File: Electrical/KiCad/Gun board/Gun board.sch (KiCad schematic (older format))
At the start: 13 parts

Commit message: created 5v, 3v3, and 3v regulator circuits
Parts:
- added C? (x2): 4.7μF, symbol Device:C
- added C?: C, symbol Device:C
- added L?: 4.7μH, symbol Device:L
- added LD? (x5): Laserdiode_1C2A, symbol Device:Laserdiode_1C2A
- added R?: 1.02MΩ, symbol Device:R
- added R?: 332kΩ, symbol Device:R
- added R?: 1MΩ, symbol Device:R
- added R?: 270Ω, symbol Device:R
- added R?: 390Ω, symbol Device:R
- added SW?: SW_SPST, symbol Switch:SW_SPST
- added U?: AAT1217, SOT23-6, symbol aat1217.lib:AAT1217
- added U?: LM317_3PinPackage, symbol Regulator_Linear:LM317_3PinPackage
- C? (x2): value C -> 4.7μF
- D?: value D_Schottky -> MBR0520
- L?: value L -> 4.7μH
- Q?: value Q_PMOS_DGS -> Si2305 DS
- R? (x2): value R -> 510kΩ
- R?: value R -> 1.02MΩ
- R?: value R -> 332kΩ
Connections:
- net labels added: +3V, +5V, +BATT, 5V_SHDN, I2C_SCL, I2C_SDA, MISO, MOSI, SCK, SELECT, SYS_SWCLK, SYS_SWDIO, TRIGGER, VOLUME
- net labels removed: ON\OFF
- wire segments 27 -> 45
- no-connect marks 0 -> 1
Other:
- note added: "Laser Diode Array"
- moved on the sheet: BT?, C?, D?, L?, Q?, R?

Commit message: added power decoupling and nets
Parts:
- removed C? (x4): 4.7μF, symbol Device:C
- removed C?: C, symbol Device:C
- added C? (x2): 100nF, symbol Device:C
- added C? (x5): 4.7μF, symbol Device:CP
- added C? (x2): 1μF, symbol Device:CP
- added C?: 10nF, symbol Device:C
- added J?: Conn_01x05, symbol Connector_Generic:Conn_01x05
- added R?: 10kΩ, symbol Device:R
- U? (x2): symbol aat1217.lib:AAT1217 -> Gun-board-rescue:AAT1217-aat1217.lib
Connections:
- net labels added: CE, CSN, RESET, VDD, VDDA
- wire segments 45 -> 88
- no-connect marks 1 -> 0
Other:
- note added: "ST LINK"
- moved on the sheet: LD?

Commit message: added current-limiting resistors to laser diodes, jumper to laser diode power supply
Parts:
- added JP?: Jumper, symbol Device:Jumper_NC_Small
- added R? (x5): 22Ω, symbol Device:R
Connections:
- wire segments 88 -> 87
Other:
- moved on the sheet: C?, R?, U?
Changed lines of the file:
@@
 L Regulator_Linear:LM317_3PinPackage U?
 U 1 1 5CBF4052
-P 1700 4750
-F 0 "U?" H 1700 4992 50  0000 C CNN
-F 1 "LM317_3PinPackage" H 1700 4901 50  0000 C CNN
-F 2 "" H 1700 5000 50  0001 C CIN
-F 3 "http://www.ti.com/lit/ds/symlink/lm317.pdf" H 1700 4750 50  0001 C CNN
-	1    1700 4750
+P 1650 4800
+F 0 "U?" H 1650 5042 50  0000 C CNN
+F 1 "LM317_3PinPackage" H 1650 4951 50  0000 C CNN
+F 2 "" H 1650 5050 50  0001 C CIN
+F 3 "http://www.ti.com/lit/ds/symlink/lm317.pdf" H 1650 4800 50  0001 C CNN
+	1    1650 4800
 	1    0    0    -1
 $EndComp
@@
 L power:+3.3V #PWR?
 U 1 1 5CBF526B
-P 1000 4750
-F 0 "#PWR?" H 1000 4600 50  0001 C CNN
-F 1 "+3.3V" H 1015 4923 50  0000 C CNN
-F 2 "" H 1000 4750 50  0001 C CNN
-F 3 "" H 1000 4750 50  0001 C CNN
-	1    1000 4750
+P 650 4800
+F 0 "#PWR?" H 650 4650 50  0001 C CNN
+F 1 "+3.3V" H 665 4973 50  0000 C CNN
+F 2 "" H 650 4800 50  0001 C CNN
+F 3 "" H 650 4800 50  0001 C CNN
+	1    650  4800
 	1    0    0    -1
 $EndComp
@@
 L Gun-board-rescue:+3V-custom_power #PWR?
 U 1 1 5CBFAAE2
-P 2600 4750
-F 0 "#PWR?" H 2600 4600 50  0001 C CNN
-F 1 "+3V" H 2615 4923 50  0000 C CNN
-F 2 "" H 2600 4750 50  0001 C CNN
-F 3 "" H 2600 4750 50  0001 C CNN
-	1    2600 4750
+P 2550 4800
+F 0 "#PWR?" H 2550 4650 50  0001 C CNN
+F 1 "+3V" H 2565 4973 50  0000 C CNN
+F 2 "" H 2550 4800 50  0001 C CNN
+F 3 "" H 2550 4800 50  0001 C CNN
+	1    2550 4800
 	1    0    0    -1
 $EndComp
@@
 L Device:R R?
 U 1 1 5CBFCB63
-P 2150 4900
-F 0 "R?" H 2220 4946 50  0000 L CNN
-F 1 "270Ω" H 2220 4855 50  0000 L CNN
-F 2 "" V 2080 4900 50  0001 C CNN
-F 3 "~" H 2150 4900 50  0001 C CNN
-	1    2150 4900
+P 2100 4950
+F 0 "R?" H 2170 4996 50  0000 L CNN
+F 1 "270Ω" H 2170 4905 50  0000 L CNN
+F 2 "" V 2030 4950 50  0001 C CNN
+F 3 "~" H 2100 4950 50  0001 C CNN
+	1    2100 4950
 	1    0    0    -1
 $EndComp
@@
 L Device:R R?
 U 1 1 5CBFD245
-P 2150 5200
-F 0 "R?" H 2220 5246 50  0000 L CNN
-F 1 "390Ω" H 2220 5155 50  0000 L CNN
-F 2 "" V 2080 5200 50  0001 C CNN
-F 3 "~" H 2150 5200 50  0001 C CNN
-	1    2150 5200
-	1    0    0    -1
-$EndComp
-Wire Wire Line
-	2000 4750 2150 4750
-Connection ~ 2150 4750
-Wire Wire Line
-	2150 5050 1700 5050
-Connection ~ 2150 5050
+P 2100 5250
+F 0 "R?" H 2170 5296 50  0000 L CNN
+F 1 "390Ω" H 2170 5205 50  0000 L CNN
+F 2 "" V 2030 5250 50  0001 C CNN
+F 3 "~" H 2100 5250 50  0001 C CNN
+	1    2100 5250
+	1    0    0    -1
+$EndComp
+Wire Wire Line
+	1950 4800 2100 4800
+Connection ~ 2100 4800
+Wire Wire Line
+	2100 5100 1650 5100
+Connection ~ 2100 5100
 $Comp
 L Gun-board-rescue:GND-custom_power #PWR?
 U 1 1 5CBFEF57
-P 2150 5350
-F 0 "#PWR?" H 2150 5100 50  0001 C CNN
-F 1 "GND" H 2155 5177 50  0000 C CNN
-F 2 "" H 2150 5350 50  0001 C CNN
-F 3 "" H 2150 5350 50  0001 C CNN
-	1    2150 5350
-	1    0    0    -1
-$EndComp
-Wire Wire Line
-	1000 4750 1400 4750
-Wire Wire Line
-	2150 4750 2600 4750
+P 2100 5400
+F 0 "#PWR?" H 2100 5150 50  0001 C CNN
+F 1 "GND" H 2105 5227 50  0000 C CNN
+F 2 "" H 2100 5400 50  0001 C CNN
+F 3 "" H 2100 5400 50  0001 C CNN
+	1    2100 5400
+	1    0    0    -1
+$EndComp
+Wire Wire Line
+	2100 4800 2550 4800
 $Comp
 L Gun-board-rescue:GND-custom_power #PWR?
 U 1 1 5CC02426
-P 2600 5050
-F 0 "#PWR?" H 2600 4800 50  0001 C CNN
-F 1 "GND" H 2605 4877 50  0000 C CNN
-F 2 "" H 2600 5050 50  0001 C CNN
-F 3 "" H 2600 5050 50  0001 C CNN
-	1    2600 5050
+P 2550 5100
+F 0 "#PWR?" H 2550 4850 50  0001 C CNN
+F 1 "GND" H 2555 4927 50  0000 C CNN
+F 2 "" H 2550 5100 50  0001 C CNN
+F 3 "" H 2550 5100 50  0001 C CNN
+	1    2550 5100
 	1    0    0    -1
 $EndComp
@@
 L Gun-board-rescue:+3V-custom_power #PWR?
 U 1 1 5CC0972E
-P 4650 6800
-F 0 "#PWR?" H 4650 6650 50  0001 C CNN
-F 1 "+3V" H 4665 6973 50  0000 C CNN
-F 2 "" H 4650 6800 50  0001 C CNN
-F 3 "" H 4650 6800 50  0001 C CNN
-	1    4650 6800
+P 4650 6500
+F 0 "#PWR?" H 4650 6350 50  0001 C CNN
+F 1 "+3V" H 4665 6673 50  0000 C CNN
+F 2 "" H 4650 6500 50  0001 C CNN
+F 3 "" H 4650 6500 50  0001 C CNN
+	1    4650 6500
 	1    0    0    -1
 $EndComp
@@
 $EndComp
 Wire Wire Line
-	3650 6950 4150 6950
-Wire Wire Line
-	4650 6950 4150 6950
-Connection ~ 4150 6950
-Wire Wire Line
-	4650 6950 5150 6950
-Connection ~ 4650 6950
-Wire Wire Line
-	5150 6950 5650 6950
-Connection ~ 5150 6950
-Wire Wire Line
 	5650 7450 5150 7450
 Wire Wire Line
@@
 	4650 7450 4650 7650
 Wire Wire Line
-	4650 6800 4650 6950
-Text Notes 3650 6800 0    50   ~ 0
+	4650 6500 4650 6650
+Text Notes 3650 6500 0    50   ~ 0
 Laser Diode Array
 Text Label 7650 2200 0    50   ~ 0
@@
 L Device:CP C?
 U 1 1 5CB5FE64
-P 2600 4900
-F 0 "C?" H 2718 4946 50  0000 L CNN
-F 1 "1μF" H 2718 4855 50  0000 L CNN
-F 2 "" H 2638 4750 50  0001 C CNN
-F 3 "~" H 2600 4900 50  0001 C CNN
-	1    2600 4900
-	1    0    0    -1
-$EndComp
-Connection ~ 2600 4750
+P 2550 4950
+F 0 "C?" H 2668 4996 50  0000 L CNN
+F 1 "1μF" H 2668 4905 50  0000 L CNN
+F 2 "" H 2588 4800 50  0001 C CNN
+F 3 "~" H 2550 4950 50  0001 C CNN
+	1    2550 4950
+	1    0    0    -1
+$EndComp
+Connection ~ 2550 4800
 Wire Wire Line
 	1250 6450 1250 6550
@@
 Wire Wire Line
 	1050 6150 1250 6150
-$Comp
-L power:VDD #PWR?
-U 1 1 5CB751D9
-P 3100 7150
-F 0 "#PWR?" H 3100 7000 50  0001 C CNN
-F 1 "VDD" H 3117 7323 50  0000 C CNN
-F 2 "" H 3100 7150 50  0001 C CNN
-F 3 "" H 3100 7150 50  0001 C CNN
-	1    3100 7150
-	1    0    0    -1
-$EndComp
 Connection ~ 2400 6150
 Wire Wire Line
@@
 Wire Wire Line
 	6450 2200 6550 2200
+$Comp
+L Device:R R?
+U 1 1 5CB6CB35
+P 3650 6800
+F 0 "R?" H 3720 6846 50  0000 L CNN
+F 1 "22Ω" H 3720 6755 50  0000 L CNN
+F 2 "" V 3580 6800 50  0001 C CNN
+F 3 "~" H 3650 6800 50  0001 C CNN
+	1    3650 6800
+	1    0    0    -1
+$EndComp
+Connection ~ 4650 6650
+Wire Wire Line
+	3650 6650 4650 6650
+Wire Wire Line
+	4650 6650 5650 6650
+$Comp
+L Device:R R?
+U 1 1 5CB932C8
+P 4150 6800
+F 0 "R?" H 4220 6846 50  0000 L CNN
+F 1 "22Ω" H 4220 6755 50  0000 L CNN
+F 2 "" V 4080 6800 50  0001 C CNN
+F 3 "~" H 4150 6800 50  0001 C CNN
+	1    4150 6800
+	1    0    0    -1
+$EndComp
+$Comp
+L Device:R R?
+U 1 1 5CB9533D
+P 4650 6800
+F 0 "R?" H 4720 6846 50  0000 L CNN
+F 1 "22Ω" H 4720 6755 50  0000 L CNN
+F 2 "" V 4580 6800 50  0001 C CNN
+F 3 "~" H 4650 6800 50  0001 C CNN
+	1    4650 6800
+	1    0    0    -1
+$EndComp
+$Comp
+L Device:R R?
+U 1 1 5CB973AF
+P 5150 6800
+F 0 "R?" H 5220 6846 50  0000 L CNN
+F 1 "22Ω" H 5220 6755 50  0000 L CNN
+F 2 "" V 5080 6800 50  0001 C CNN
+F 3 "~" H 5150 6800 50  0001 C CNN
+	1    5150 6800
+	1    0    0    -1
+$EndComp
+$Comp
+L Device:R R?
+U 1 1 5CB99428
+P 5650 6800
+F 0 "R?" H 5720 6846 50  0000 L CNN
+F 1 "22Ω" H 5720 6755 50  0000 L CNN
+F 2 "" V 5580 6800 50  0001 C CNN
+F 3 "~" H 5650 6800 50  0001 C CNN
+	1    5650 6800
+	1    0    0    -1
+$EndComp
+$Comp
+L Device:Jumper_NC_Small JP?
+U 1 1 5CB7DD44
+P 1000 4800
+F 0 "JP?" H 1000 5012 50  0000 C CNN
+F 1 "Jumper" H 1000 4921 50  0000 C CNN
+F 2 "" H 1000 4800 50  0001 C CNN
+F 3 "~" H 1000 4800 50  0001 C CNN
+	1    1000 4800
+	1    0    0    -1
+$EndComp
+Wire Wire Line
+	1100 4800 1350 4800
+Wire Wire Line
+	650  4800 900  4800
 $EndSCHEMATC

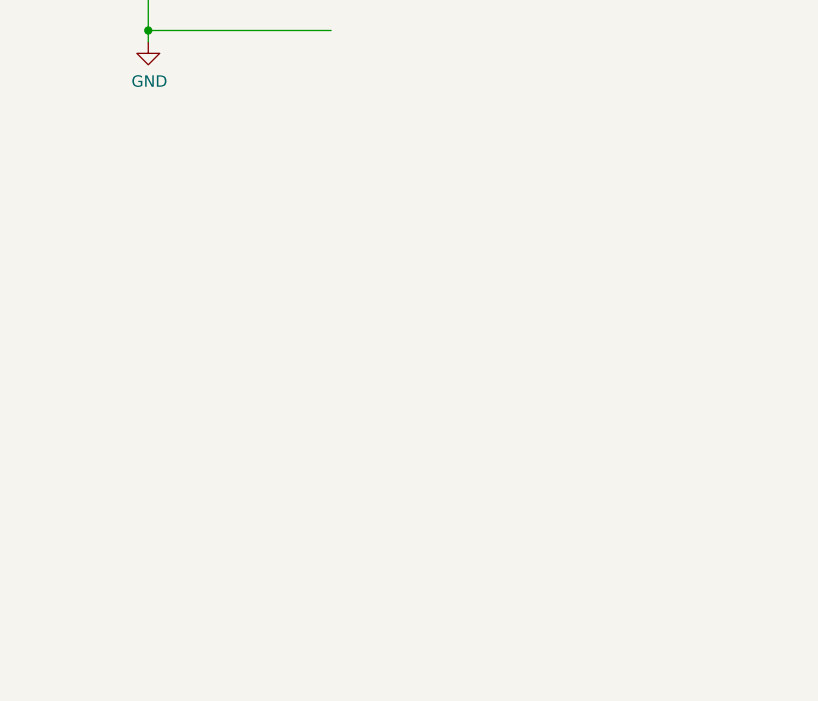
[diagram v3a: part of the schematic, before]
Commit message: added NRF24L01 breakout module
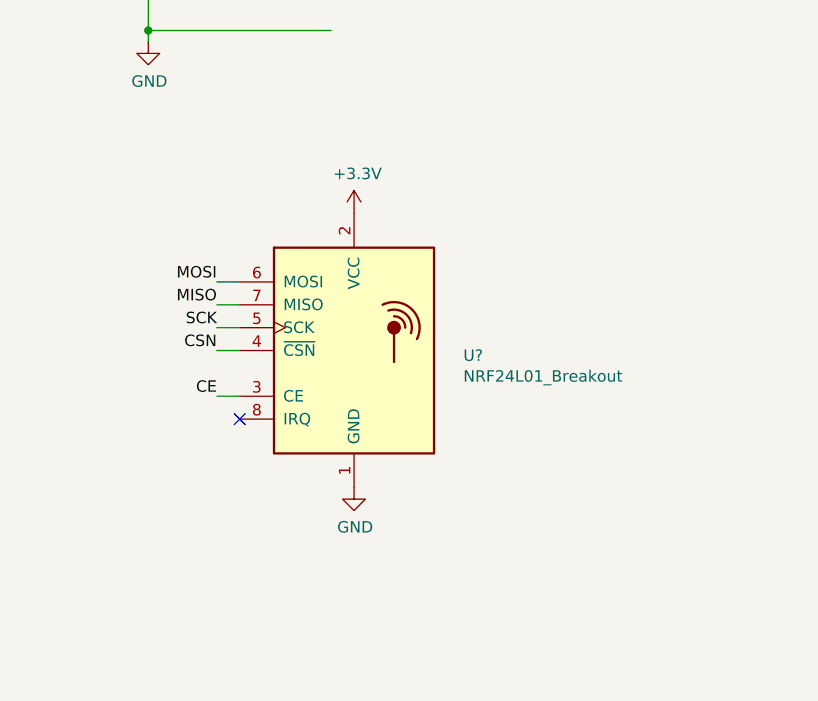
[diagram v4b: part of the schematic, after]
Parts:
- added U?: NRF24L01_Breakout, RF_Module:nRF24L01_Breakout, symbol RF:NRF24L01_Breakout
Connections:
- wire segments 87 -> 92
- no-connect marks 0 -> 1

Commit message: Switched LED Driver IC to directly-controlled BJTs
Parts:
- added D? (x2): LED, symbol Device:LED
- added JP?: Jumper, symbol Device:Jumper_NC_Small
- added Q? (x2): 2N3904, Package_TO_SOT_THT:TO-92_Inline, symbol Transistor_BJT:2N3904
- added R? (x4): 10kΩ, symbol Device:R
- added R? (x2): 100Ω, symbol Device:R
- added SW?: SW_SPST, symbol Switch:SW_SPST
- U? (x2): symbol Gun-board-rescue:AAT1217-aat1217.lib -> Gun-board-rescue:AAT1217-aat1217.lib-Gun-board-rescue
- U?: symbol MCU_ST_STM32F0:STM32F030F4Px -> Gun-board-rescue:STM32F030F4Px-MCU_ST_STM32F0
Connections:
- net labels added: LED1, LED2
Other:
- note added: "BARREL LEDS"
- moved on the sheet: R?, U?

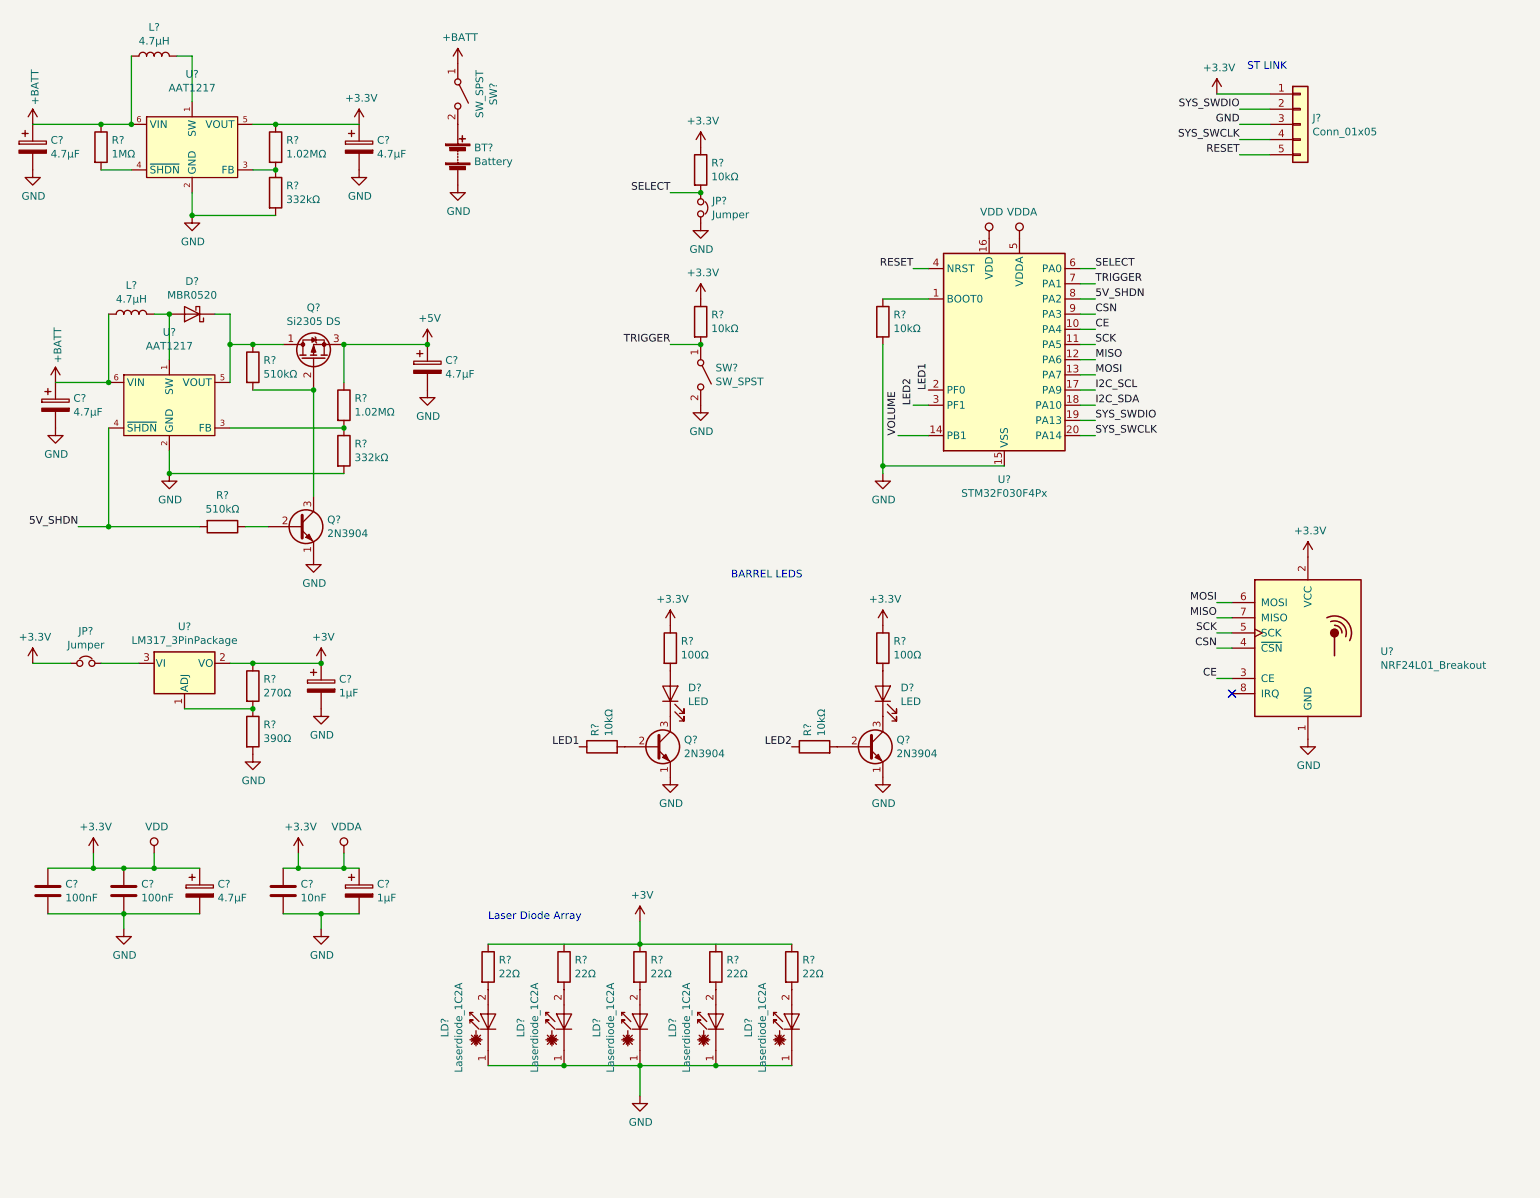
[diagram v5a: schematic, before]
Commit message: added volume control input
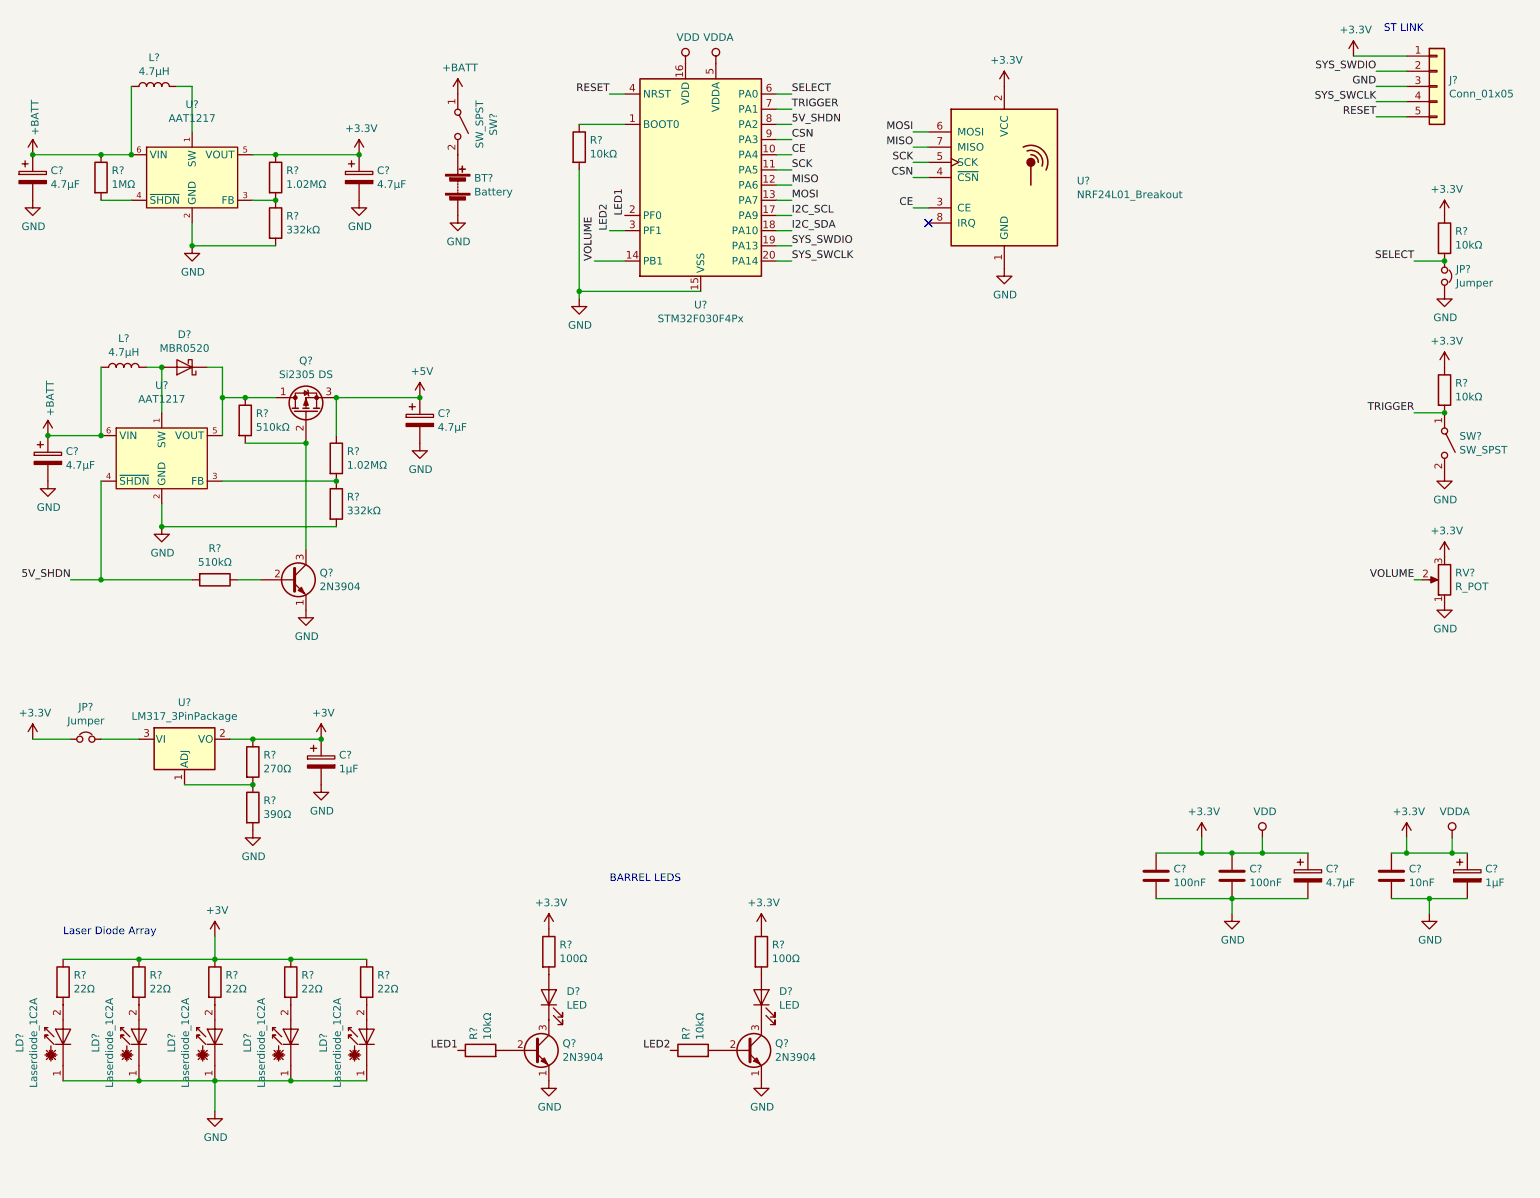
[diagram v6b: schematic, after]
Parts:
- added RV?: R_POT, symbol Device:R_POT
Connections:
- net +3V3: now also RV?.3
- net +4V: now also R?.1, R?.1
- net GND: now also RV?.1
- net VOLUME: now also RV?.2
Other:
- moved on the sheet: BT?, C?, D?, J?, JP?, L?, LD?, Q?, R?, SW?, U?

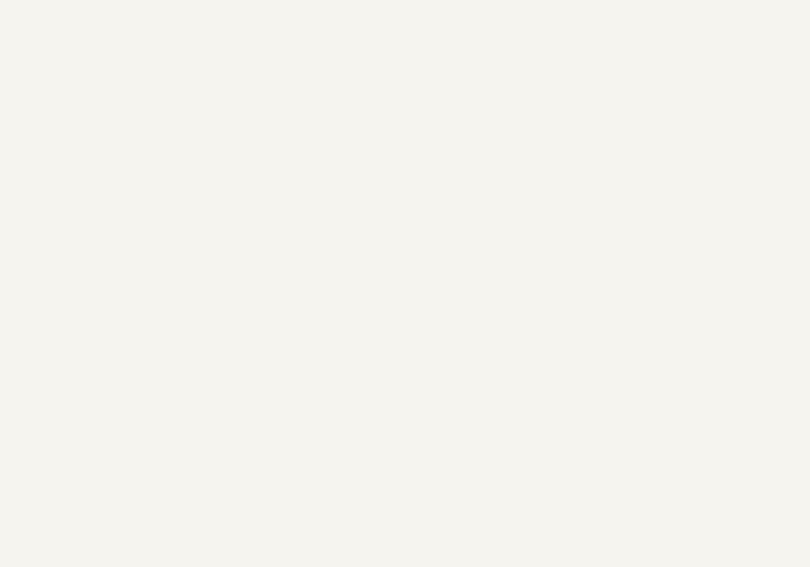
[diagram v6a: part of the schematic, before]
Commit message: created MCP4725 on schematic
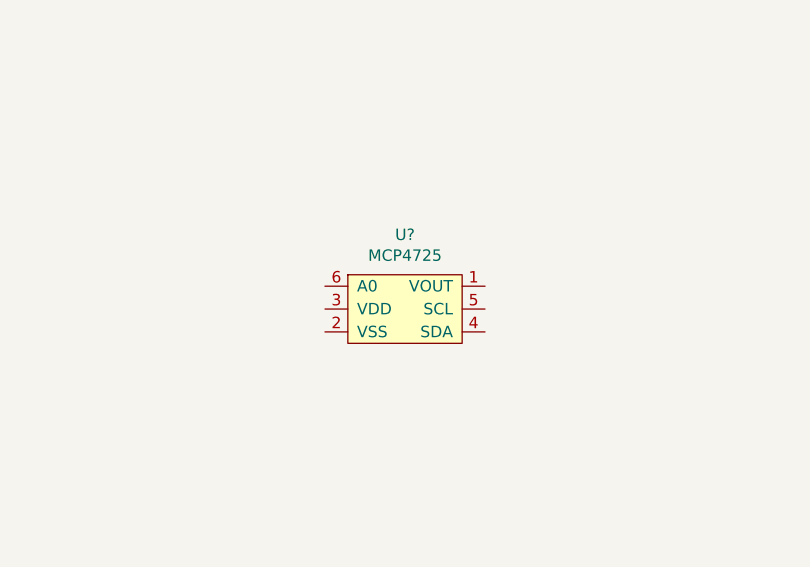
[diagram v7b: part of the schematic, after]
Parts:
- added U?: MCP4725, symbol custom_components:MCP4725
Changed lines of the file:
@@
 Wire Wire Line
 	9750 4250 9800 4250
+$Comp
+L custom_components:MCP4725 U?
+U 1 1 5CE30293
+P 5750 4300
+F 0 "U?" H 5750 4625 50  0000 C CNN
+F 1 "MCP4725" H 5750 4534 50  0000 C CNN
+F 2 "" H 5750 4500 50  0001 C CNN
+F 3 "" H 5750 4500 50  0001 C CNN
+	1    5750 4300
+	1    0    0    -1
+$EndComp
 $EndSCHEMATC
